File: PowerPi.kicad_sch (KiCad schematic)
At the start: 34 parts, among them J1 2444, J3 Conn_01x02, J6 Raspberry_Pi_2_3, J8 2444, Q1 30V 4A 44mΩ, Q2 50nA 150V 200mW 200mA, Q3 30V 4A 44mΩ, U1 XL4015

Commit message: improved copper balance
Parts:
- C2, C3: footprint Capacitor_SMD:C_0402_1005Metric -> Capacitor_SMD:C_0603_1608Metric; LCSC (none) -> C15849; ManfNum (none) -> CL10A105KB8NNNC; PCBway (none) -> CL10A105KB8NNNC; abv.Footprint 0402 -> 0603
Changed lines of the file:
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@@
       (effects (font (size 1.27 1.27)) (justify right))
     )
-    (property "Footprint" "Capacitor_SMD:C_0402_1005Metric" (id 2) (at 77.978 98.171 0)
+    (property "Footprint" "Capacitor_SMD:C_0603_1608Metric" (id 2) (at 77.978 98.171 0)
       (effects (font (size 1.27 1.27)) hide)
     )
@@
       (effects (font (size 1.27 1.27)) hide)
     )
-    (property "LCSC" "" (id 4) (at 77.978 98.171 0)
-      (effects (font (size 1.27 1.27)) hide)
-    )
-    (property "PCBway" "" (id 5) (at 77.978 98.171 0)
-      (effects (font (size 1.27 1.27)) hide)
-    )
-    (property "abv.Footprint" "0402" (id 6) (at 77.978 98.171 0)
-      (effects (font (size 1.27 1.27)) hide)
-    )
-    (property "ManfNum" "" (id 7) (at 77.978 98.171 0)
+    (property "LCSC" "C15849" (id 4) (at 77.978 98.171 0)
+      (effects (font (size 1.27 1.27)) hide)
+    )
+    (property "PCBway" "CL10A105KB8NNNC" (id 5) (at 77.978 98.171 0)
+      (effects (font (size 1.27 1.27)) hide)
+    )
+    (property "abv.Footprint" "0603" (id 6) (at 77.978 98.171 0)
+      (effects (font (size 1.27 1.27)) hide)
+    )
+    (property "ManfNum" "CL10A105KB8NNNC" (id 7) (at 77.978 98.171 0)
       (effects (font (size 1.27 1.27)) hide)
     )
@@
       (effects (font (size 1.27 1.27)) (justify left))
     )
-    (property "Footprint" "Capacitor_SMD:C_0402_1005Metric" (id 2) (at 67.7164 98.171 0)
+    (property "Footprint" "Capacitor_SMD:C_0603_1608Metric" (id 2) (at 67.7164 98.171 0)
       (effects (font (size 1.27 1.27)) hide)
     )
@@
       (effects (font (size 1.27 1.27)) hide)
     )
-    (property "LCSC" "" (id 4) (at 67.7164 98.171 0)
-      (effects (font (size 1.27 1.27)) hide)
-    )
-    (property "PCBway" "" (id 5) (at 67.7164 98.171 0)
-      (effects (font (size 1.27 1.27)) hide)
-    )
-    (property "abv.Footprint" "0402" (id 6) (at 67.7164 98.171 0)
-      (effects (font (size 1.27 1.27)) hide)
-    )
-    (property "ManfNum" "" (id 7) (at 67.7164 98.171 0)
+    (property "LCSC" "C15849" (id 4) (at 67.7164 98.171 0)
+      (effects (font (size 1.27 1.27)) hide)
+    )
+    (property "PCBway" "CL10A105KB8NNNC" (id 5) (at 67.7164 98.171 0)
+      (effects (font (size 1.27 1.27)) hide)
+    )
+    (property "abv.Footprint" "0603" (id 6) (at 67.7164 98.171 0)
+      (effects (font (size 1.27 1.27)) hide)
+    )
+    (property "ManfNum" "CL10A105KB8NNNC" (id 7) (at 67.7164 98.171 0)
       (effects (font (size 1.27 1.27)) hide)
     )
@@
     )
     (path "/3427c5b8-85a9-4bc0-9950-3d8f93e645b4"
-      (reference "C2") (unit 1) (value "1 uF") (footprint "Capacitor_SMD:C_0402_1005Metric")
+      (reference "C2") (unit 1) (value "1 uF") (footprint "Capacitor_SMD:C_0603_1608Metric")
     )
     (path "/227bddcb-c42b-4cd8-bc3e-9967b0269b8c"
-      (reference "C3") (unit 1) (value "1 uF") (footprint "Capacitor_SMD:C_0402_1005Metric")
+      (reference "C3") (unit 1) (value "1 uF") (footprint "Capacitor_SMD:C_0603_1608Metric")
     )
     (path "/19072074-aee5-4bd8-87b4-b7ee7fae14bf"

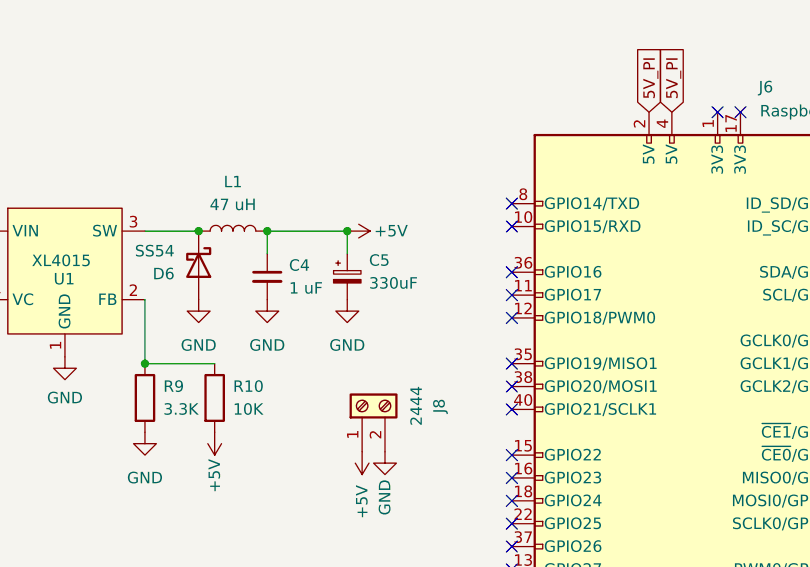
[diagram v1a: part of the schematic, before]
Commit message: update to 1000 uF output electrolytic capacitor
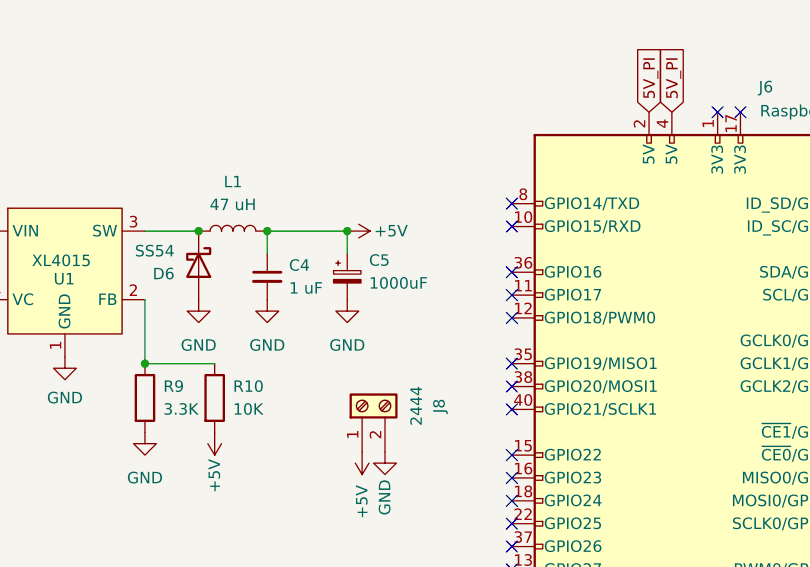
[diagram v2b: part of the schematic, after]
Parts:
- C5: value 330uF -> 1000uF; footprint Capacitor_SMD:CP_Elec_6.3x7.7 -> Capacitor_SMD:CP_Elec_8x10; LCSC C58277 -> C310838; ManfNum RVT1A331M0607 -> RVE1A102M0810; PCBway RVT1A331M0607 -> RVE1A102M0810; abv.Footprint SMD_6.3x7.7mm -> SMD-ECAP-8x10
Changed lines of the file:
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@@
       (effects (font (size 1.27 1.27)) (justify left))
     )
-    (property "Value" "330uF" (id 1) (at 126.111 101.4348 0)
-      (effects (font (size 1.27 1.27)) (justify left))
-    )
-    (property "Footprint" "Capacitor_SMD:CP_Elec_6.3x7.7" (id 2) (at 123.698 100.711 0)
+    (property "Value" "1000uF" (id 1) (at 126.111 101.4348 0)
+      (effects (font (size 1.27 1.27)) (justify left))
+    )
+    (property "Footprint" "Capacitor_SMD:CP_Elec_8x10" (id 2) (at 123.698 100.711 0)
       (effects (font (size 1.27 1.27)) hide)
     )
@@
       (effects (font (size 1.27 1.27)) hide)
     )
-    (property "LCSC" "C58277" (id 4) (at 123.698 100.711 0)
-      (effects (font (size 1.27 1.27)) hide)
-    )
-    (property "PCBway" "RVT1A331M0607" (id 5) (at 123.698 100.711 0)
-      (effects (font (size 1.27 1.27)) hide)
-    )
-    (property "abv.Footprint" "SMD_6.3x7.7mm" (id 6) (at 123.698 100.711 0)
-      (effects (font (size 1.27 1.27)) hide)
-    )
-    (property "ManfNum" "RVT1A331M0607" (id 7) (at 123.698 100.711 0)
+    (property "LCSC" "C310838" (id 4) (at 123.698 100.711 0)
+      (effects (font (size 1.27 1.27)) hide)
+    )
+    (property "PCBway" "RVE1A102M0810" (id 5) (at 123.698 100.711 0)
+      (effects (font (size 1.27 1.27)) hide)
+    )
+    (property "abv.Footprint" "SMD-ECAP-8x10" (id 6) (at 123.698 100.711 0)
+      (effects (font (size 1.27 1.27)) hide)
+    )
+    (property "ManfNum" "RVE1A102M0810" (id 7) (at 123.698 100.711 0)
       (effects (font (size 1.27 1.27)) hide)
     )
@@
     )
     (path "/858d080d-4b19-45cc-bb9f-d3c272f2a854"
-      (reference "C5") (unit 1) (value "330uF") (footprint "Capacitor_SMD:CP_Elec_6.3x7.7")
+      (reference "C5") (unit 1) (value "1000uF") (footprint "Capacitor_SMD:CP_Elec_8x10")
     )
     (path "/80adc0a2-c38b-4c02-a9a6-e9d639d0764f"
